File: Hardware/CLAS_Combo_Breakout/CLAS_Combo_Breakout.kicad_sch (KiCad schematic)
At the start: 18 parts

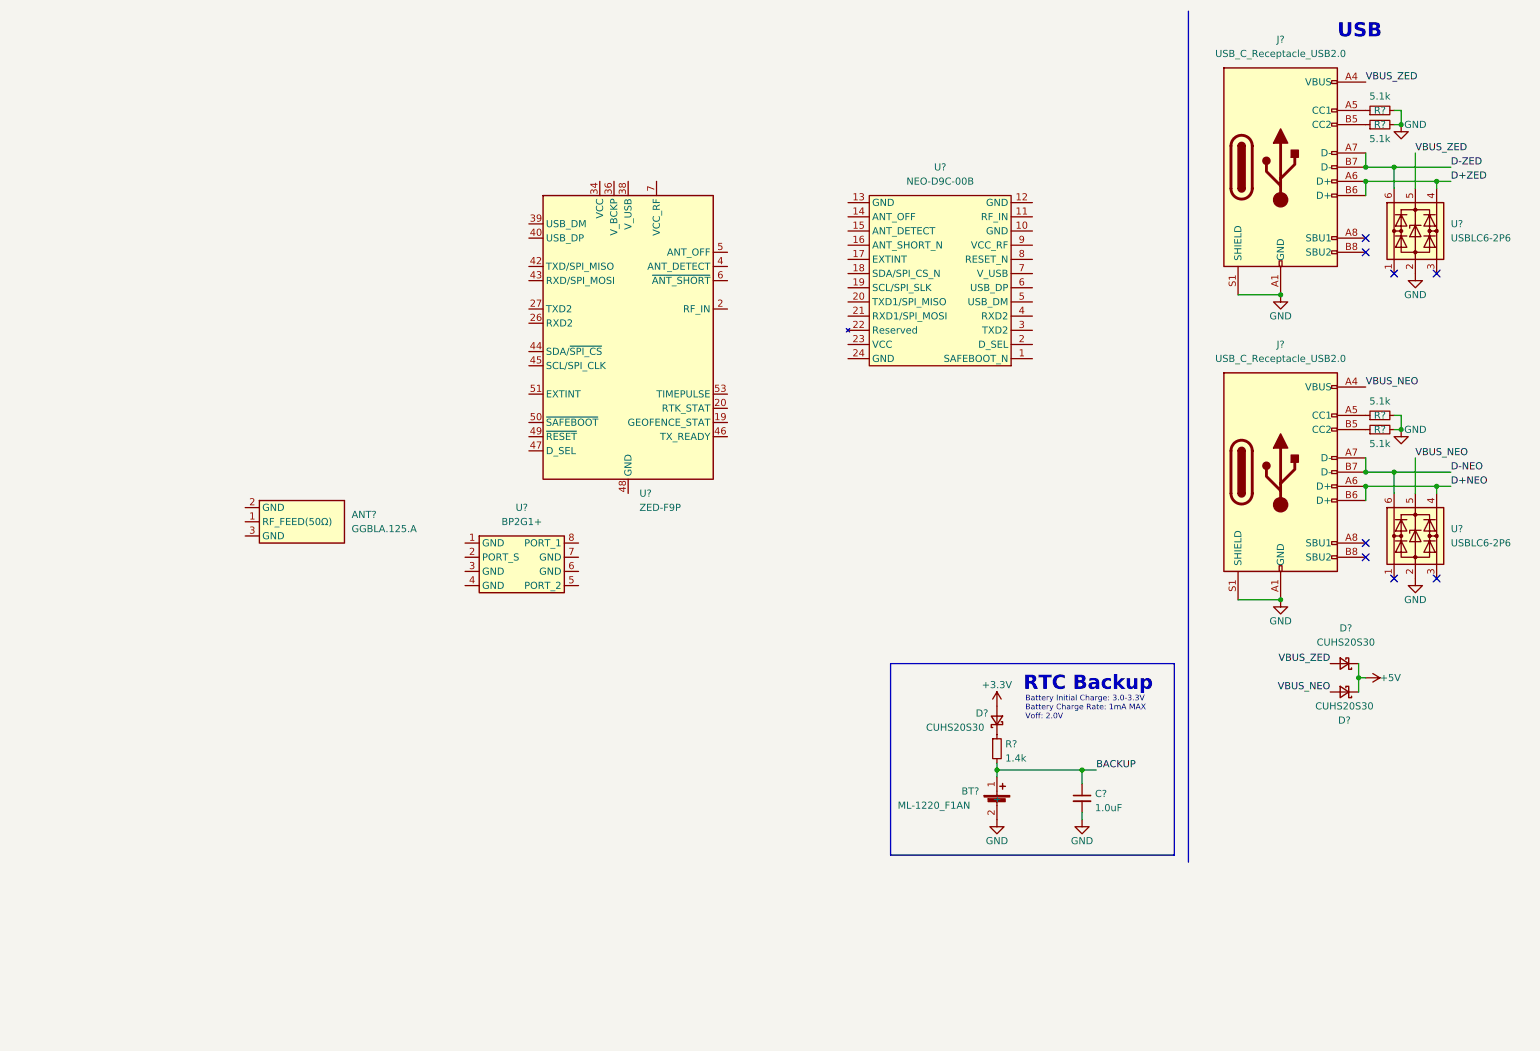
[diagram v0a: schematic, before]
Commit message: add LNA
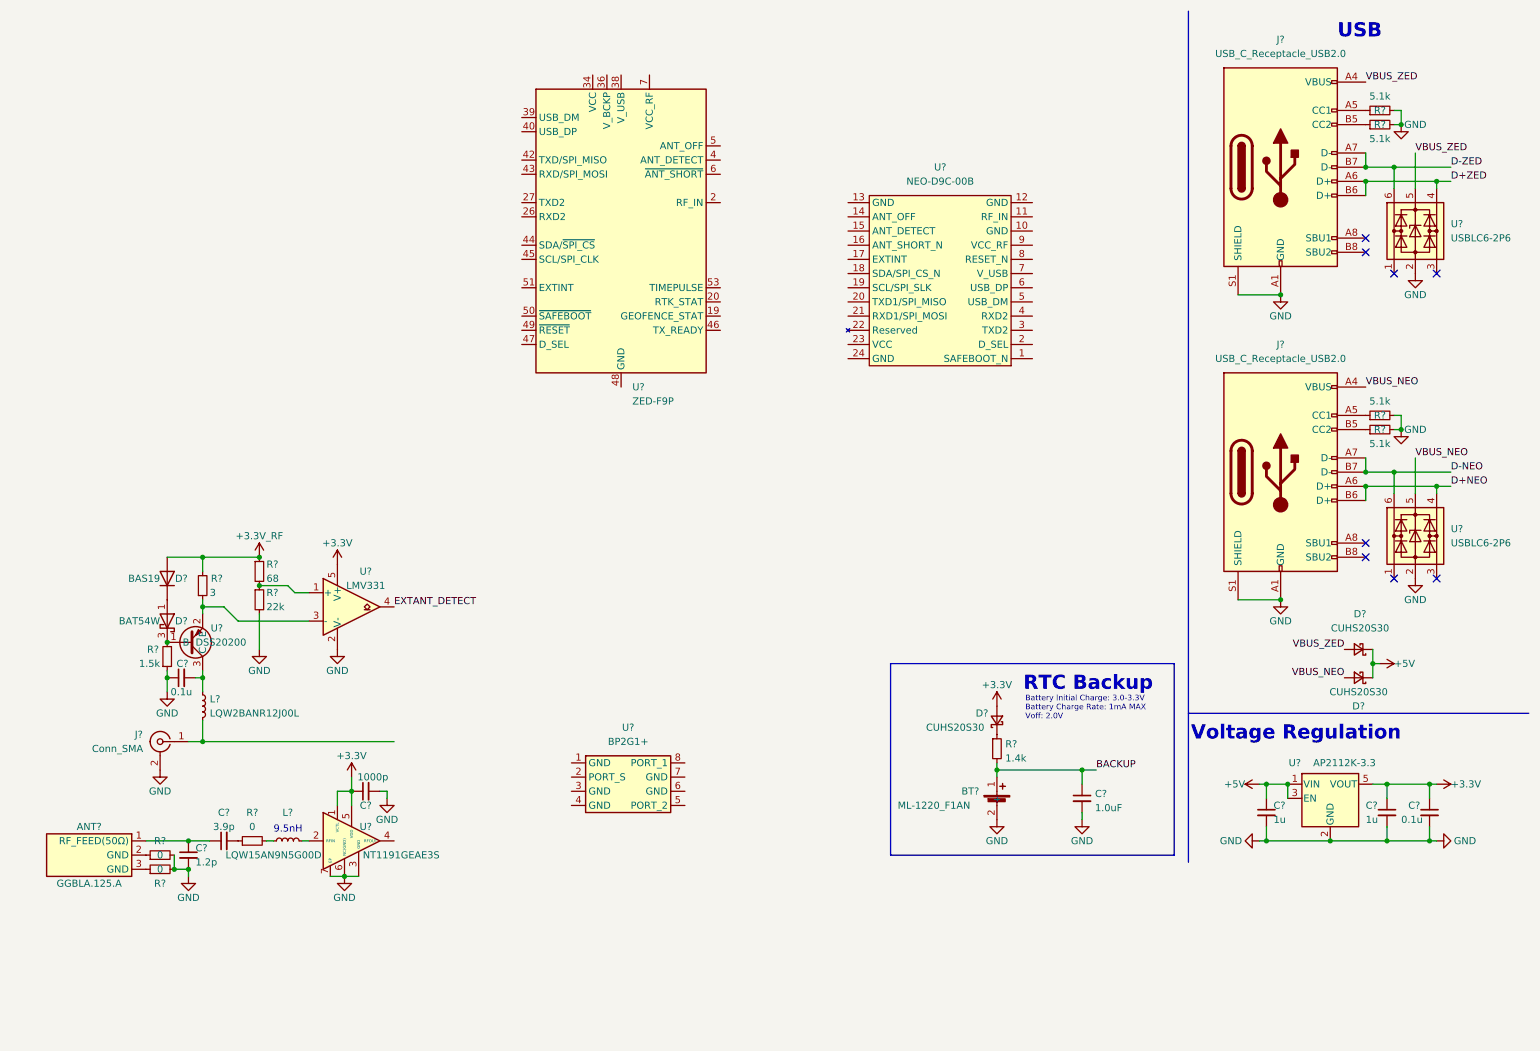
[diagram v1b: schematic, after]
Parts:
- added C? (x2): 1u, symbol Device:C_Small
- added C?: 1.2p, symbol Device:C_Small
- added C?: 3.9p, symbol Device:C_Small
- added C?: 1000p, symbol Device:C_Small
- added C? (x2): 0.1u, symbol Device:C_Small
- added D?: BAS19, Package_TO_SOT_SMD:SOT-23, symbol Diode:BAS19
- added D?: BAT54W, Package_TO_SOT_SMD:SOT-323_SC-70, symbol Diode:BAT54W
- added J?: Conn_SMA, symbol Connector:Conn_Coaxial
- added L?: LQW2BANR12J00L, symbol Device:L_Small
- added L?: LQW15AN9N5G00D, symbol Device:L_Small
- added R? (x3): 0, symbol Device:R_Small
- added R?: 68, symbol Device:R_Small
- added R?: 1.5k, symbol Device:R_Small
- added R?: 22k, symbol Device:R_Small
- added R?: 3, symbol Device:R_Small
- added U?: NT1191GEAE3S, symbol NT1191GEAE3S:NT1191GEAE3S
- added U?: AP2112K-3.3, Package_TO_SOT_SMD:SOT-23-5, symbol Regulator_Linear:AP2112K-3.3
- added U?: DSS20200, symbol DSS20200L-7:DSS20200L-7
- added U?: LMV331, symbol Comparator:LMV331
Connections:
- net +3.3V: now also C?.1, C?.1, C?.1, U?.1 (VCTL), U?.5 (V+), U?.5 (VDD), U?.5 (VOUT)
- net +5V: now also C?.1, U?.1 (VIN), U?.3 (EN)
- net GND: now also C?.1, C?.2, C?.2, C?.2, C?.2, C?.2, J?.2 (Ext), R?.1, R?.2, R?.2, R?.2, U?.2 (GND), U?.2 (V-), U?.3 (GND), U?.6 (NC(GND)), U?.7 (EP)
- net at ANT?.1 (RF_FEED(50Ω)): now also C?.1, C?.1
- net at ANT?.2 (GND): now also R?.1
- net at ANT?.3 (GND): now also R?.1
- new net: L?.2, U?.2 (RFIN)
- new net: R?.1, R?.2, U?.1 (+)
- new net: D?.1 (A), D?.3 (K)
- new net: D?.3 (K), R?.2, U?.1 (B)
- new net: C?.2, R?.1
- new net: C?.2, L?.1, U?.3 (C)
- new net: J?.1 (In), L?.2
- new net: R?.1, U?.2 (E), U?.3 (-)
- new net: L?.1, R?.2
- new net +3.3V_RF: D?.1 (A), R?.1, R?.2
- new net EXTANT_DETECT: U?.4
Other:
- note added: "9.5nH"
- note added: "Voltage Regulation"
- moved on the sheet: ANT?, D?, U?

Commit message: 受信回路完成
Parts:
- added D?: EXTANT, symbol Device:LED_Small
- added D?: PESD0402-140, symbol Device:D_TVS
- added R?: 1k, symbol Device:R_Small
- added RY?: G6K-2F-RF-S-DC3, symbol G6K-2F-RF-S-DC3:G6K-2F-RF-S-DC3
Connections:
- net EXTANT_DETECT: now also R?.1, RY?.1
- net GND: now also U?.1 (GND), U?.3 (GND), U?.4 (GND), U?.6 (GND), U?.7 (GND), D?.1 (A1), D?.1 (K), RY?.5, RY?.6, RY?.7, RY?.8, RY?.MP1 (SHIELD), RY?.MP2 (SHIELD), RY?.MP3 (SHIELD), RY?.MP4 (SHIELD), RY?.MP5 (SHIELD), RY?.MP6 (SHIELD)
- net at U?.4 (RFOUT): now also RY?.2
- net at U?.2 (S): now also RY?.3
- net ANT_NEO: now reaches U?.5 (2)
- net ANT_ZED: now reaches U?.8 (1)
- net at J?.1 (In), L?.2: now also D?.2 (A2), RY?.4
- new net: D?.2 (A), R?.2
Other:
- note added: "External active antenna detect"
- note added: "Indicator"
- note added: "RF Amplifiers"
- moved on the sheet: ANT?, BT?, C?, D?, J?, L?, R?, U?

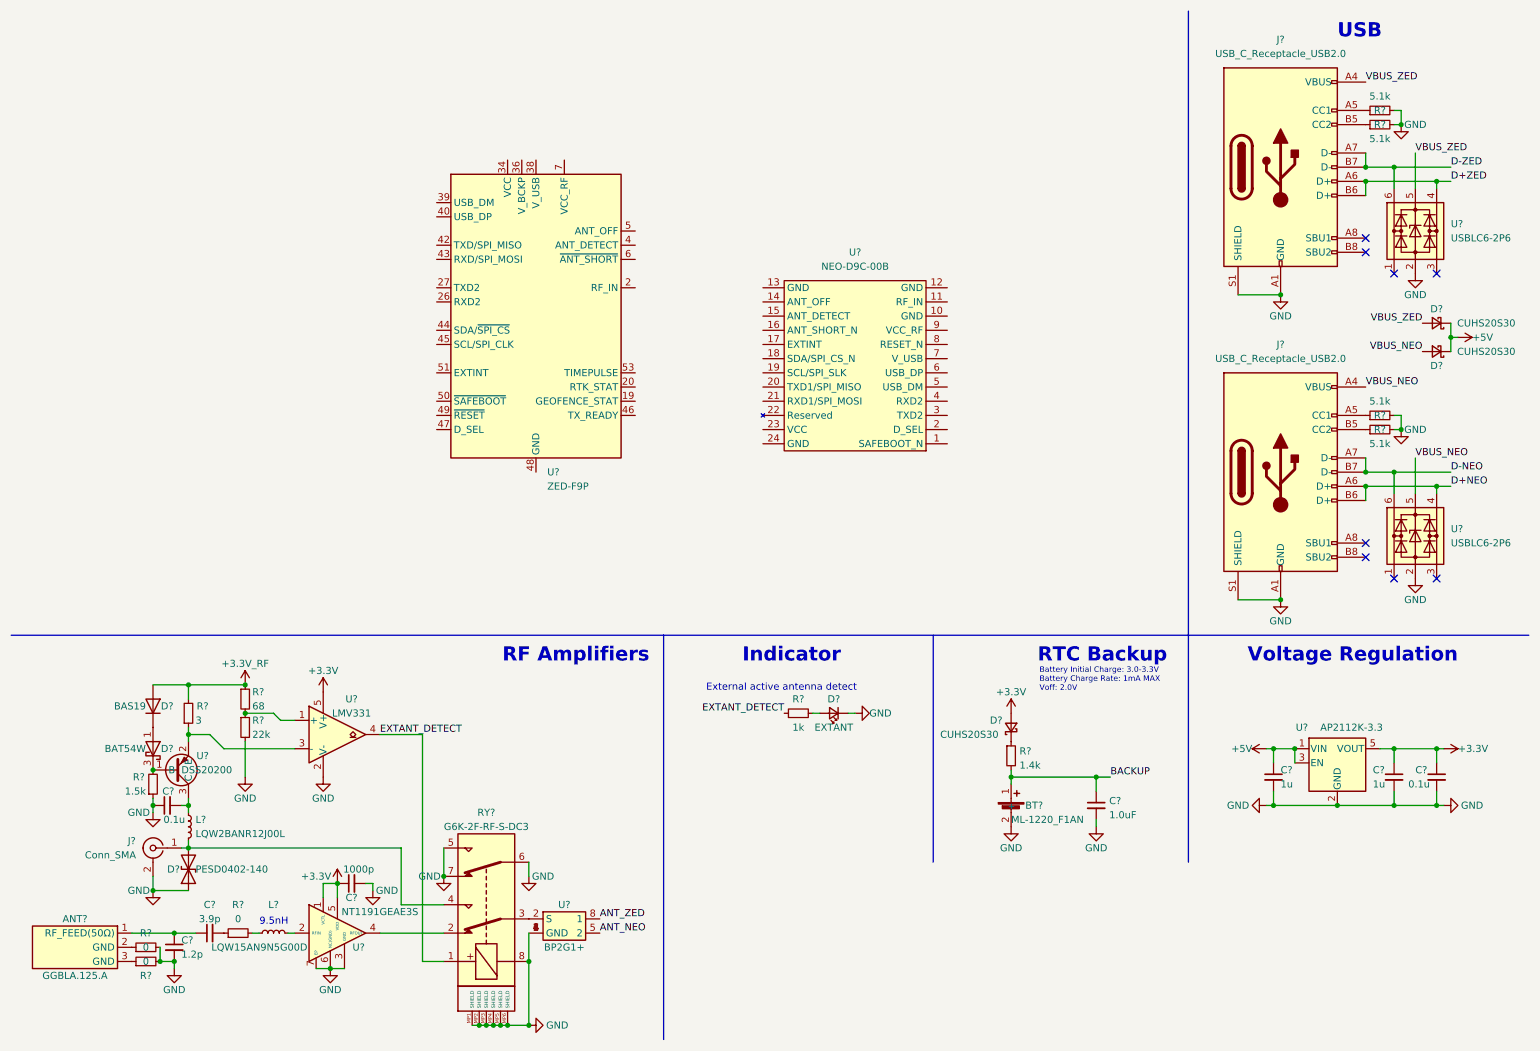
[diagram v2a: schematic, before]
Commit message: update schematic
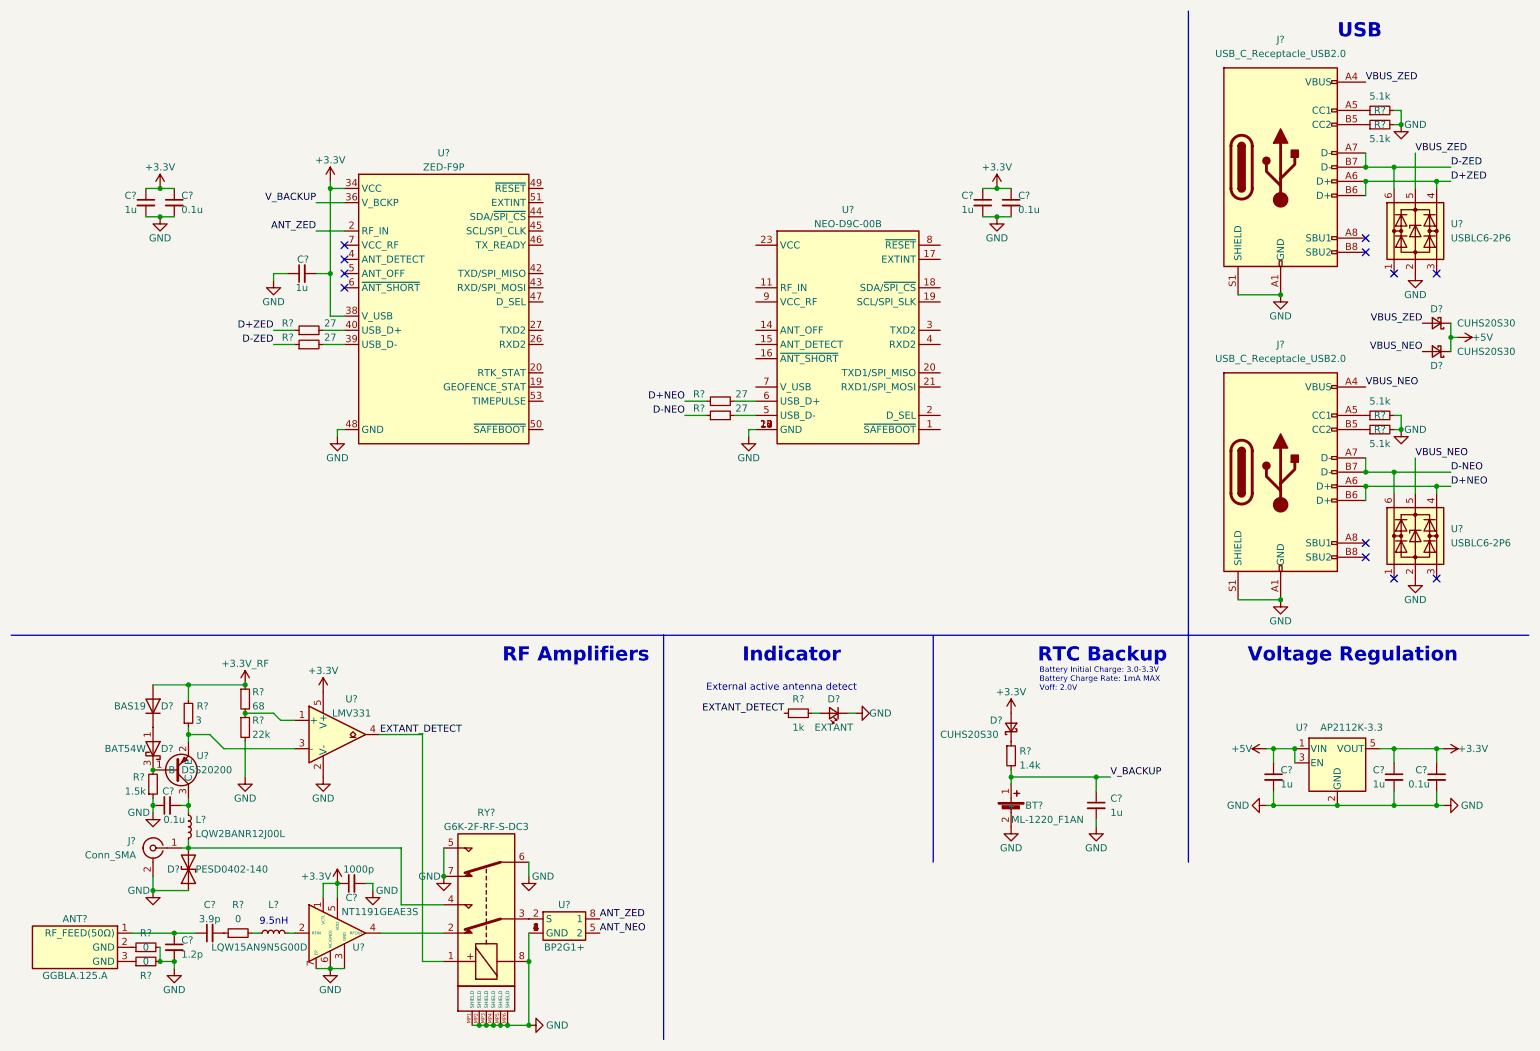
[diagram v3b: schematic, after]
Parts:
- added C? (x2): 0.1u, symbol Device:C_Small
- added C? (x3): 1u, symbol Device:C_Small
- added R? (x4): 27, symbol Device:R_Small
- C?: value 1.0uF -> 1u
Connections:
- net BACKUP is gone; now on net V_BACKUP: BT?.1 (+), C?.1, R?.2
- net +3.3V: now also U?.33 (VCC), U?.34 (VCC), U?.38 (V_USB), C?.1, C?.1, C?.1, C?.1, C?.2
- net ANT_ZED: now also U?.2 (RF_IN)
- net D+NEO: now also R?.1
- net D+ZED: now also R?.1
- net D-NEO: now also R?.1
- net D-ZED: now also R?.1
- net GND: now also U?.1 (GND), U?.10 (GND), U?.12 (GND), U?.12 (GND), U?.13 (GND), U?.14 (GND), U?.24 (GND), U?.3 (GND), U?.32 (GND), U?.37 (GND), U?.41 (GND), U?.48 (GND), U?.55 (GND), C?.1, C?.2, C?.2, C?.2, C?.2
- net at U?.5 (USB_D-): now also R?.2
- net at U?.6 (USB_D+): now also R?.2
- net at U?.10 (Reserved): now also U?.11 (Reserved), U?.13 (Reserved), U?.15 (Reserved), U?.16 (Reserved), U?.17 (Reserved), U?.18 (Reserved), U?.21 (Reserved), U?.22 (Reserved), U?.23 (Reserved), U?.24 (Reserved), U?.25 (Reserved), U?.28 (Reserved), U?.29 (Reserved), U?.30 (Reserved), U?.31 (Reserved), U?.35 (Reserved), U?.52 (Reserved), U?.54 (Reserved), U?.8 (Reserved), U?.9 (Reserved)
- net V_BACKUP: now reaches U?.36 (V_BCKP)
- net at U?.39 (USB_D-): now also R?.2
- net at U?.40 (USB_D+): now also R?.2
- no-connect marks 8 -> 12
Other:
- moved on the sheet: U?

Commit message: update schematic
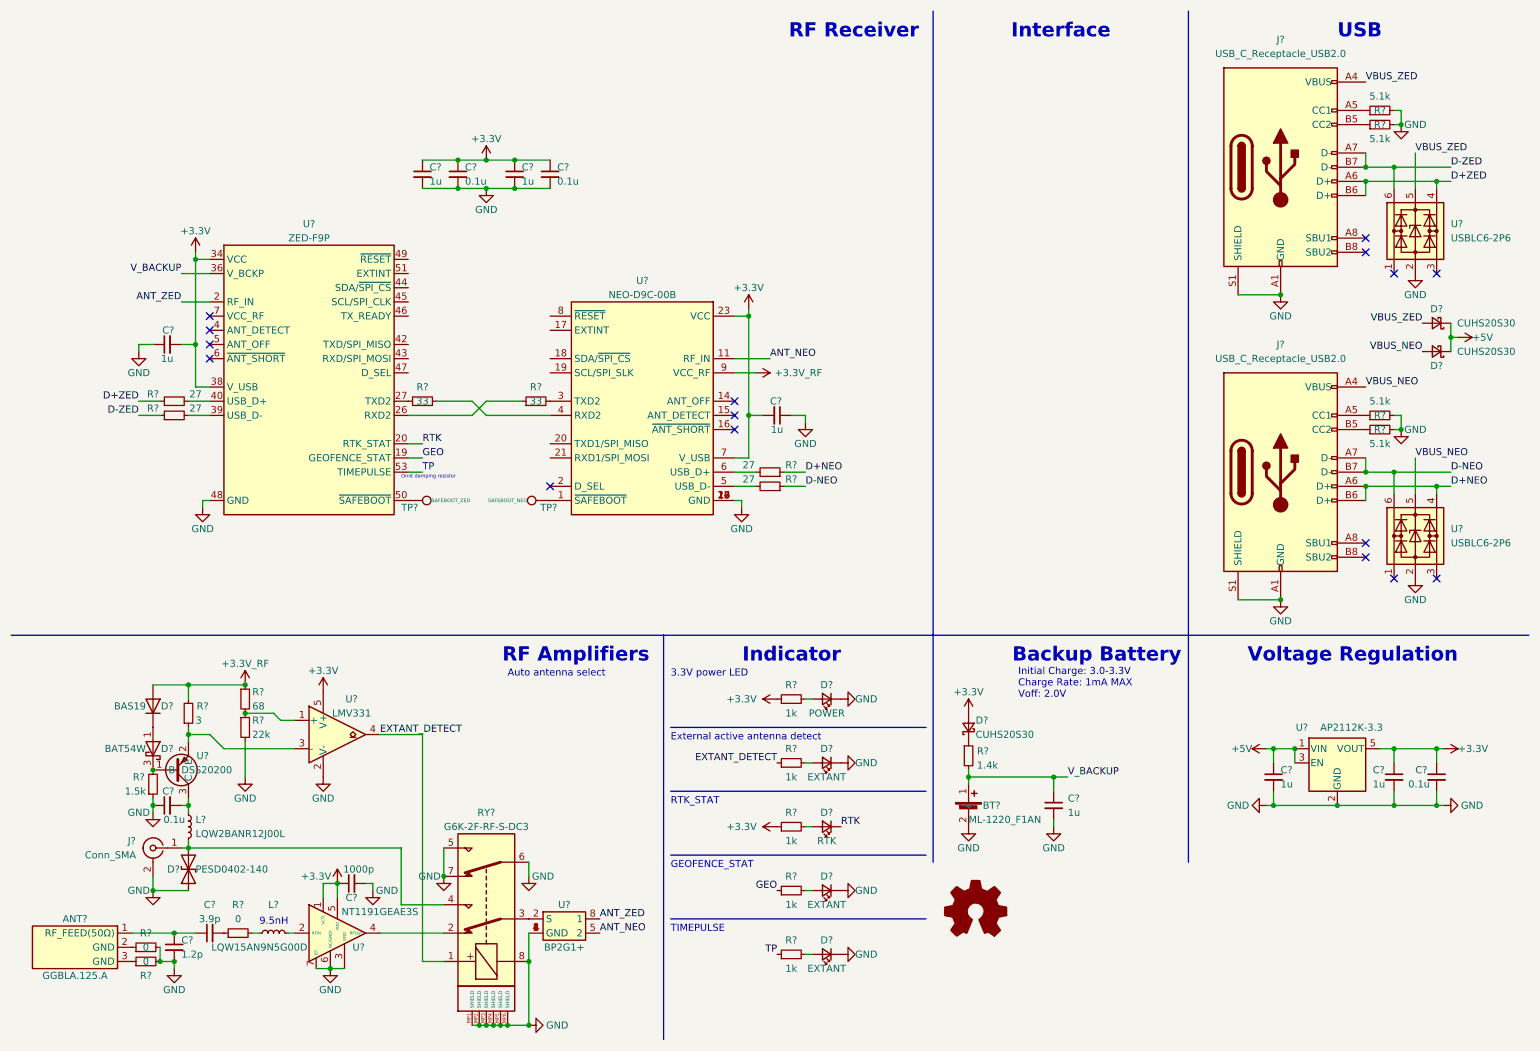
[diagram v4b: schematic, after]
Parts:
- removed C?: 0.1u, symbol Device:C_Small
- removed C?: 1u, symbol Device:C_Small
- added C?: 0.1u, symbol Device:C_Small
- added C? (x2): 1u, symbol Device:C_Small
- added D?: POWER, symbol Device:LED_Small
- added D? (x2): EXTANT, symbol Device:LED_Small
- added D?: RTK, symbol Device:LED_Small
- added R? (x4): 1k, symbol Device:R_Small
- added R? (x2): 33, symbol Device:R_Small
- added TP?: SAFEBOOT_ZED, symbol Connector:TestPoint
- added TP?: SAFEBOOT_NEO, symbol Connector:TestPoint
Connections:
- net +3.3V: now also U?.23 (VCC), U?.7 (V_USB), C?.1, C?.1, C?.2, R?.1, R?.1
- net +3.3V_RF: now also U?.9 (VCC_RF)
- net ANT_NEO: now also U?.11 (RF_IN)
- net GND: now also C?.1, C?.2, C?.2, D?.1 (K), D?.1 (K), D?.1 (K)
- net at U?.1 (~{SAFEBOOT}): now also TP?.1
- net at U?.3 (TXD2): now also R?.2
- net at U?.4 (RXD2): now also R?.2
- net GEO: now reaches U?.19 (GEOFENCE_STAT)
- net GEO: now also R?.1
- net RTK: now reaches U?.20 (RTK_STAT)
- net RTK: now also D?.1 (K)
- net at U?.26 (RXD2): now also R?.1
- net at U?.27 (TXD2): now also R?.1
- net at U?.50 (~{SAFEBOOT}): now also TP?.1
- net TP: now reaches U?.53 (TIMEPULSE)
- net TP: now also R?.1
- new net: D?.2 (A), R?.2 (x4)
- no-connect marks 12 -> 16
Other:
- note added: "3.3V power LED"
- note added: "Auto antenna select"
- note added: "Backup Battery"
- note added: "GEOFENCE_STAT"
- note added: "Initial Charge: 3.0-3.3V Charge Rate: 1mA MAX Voff: 2.0V"
- note added: "Interface"
- note added: "Omit damping resistor"
- note added: "RF Receiver"
- note added: "RTK_STAT"
- note added: "TIMEPULSE"
- note removed: "Battery Initial Charge: 3.0-3.3V Battery Charge Rate: 1mA MAX Voff: 2.0V"
- note removed: "RTC Backup"
- moved on the sheet: BT?, C?, D?, R?, U?
